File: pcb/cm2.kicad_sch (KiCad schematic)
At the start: 614 parts, among them J1 top left, J2 bottom left, J3 Raspberry_Pi_2_3, J4 Screw_Terminal_01x02, J5 Screw_Terminal_01x02, U1 HT1632C-52LQFP, U2 HT1632C-52LQFP

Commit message: update to v6.0
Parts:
- C1, C11, C12, C2: symbol Device:CP1 -> Device:C_Polarized_Small_US
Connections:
- net +5V: now also C1.1, C11.1, C12.1, C2.1
- net GND: now also C1.2, C11.2, C12.2, C2.2
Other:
- note added: "Design for either SMT or TH large caps, no need to install both! (DNP either C1, C2 or CX, CY)"
- note added: "Designed for two boards to be plugged together so that ~{CS2} and ~{CS3} of the left board (with the RPi) become ~{CS0} and ~{CS1} of the right board."
- note added: "For historical accuracy, ensure LEDS have a spectral center > 635 nM Drivers only supply ~10 mA so high-brightness LEDS such as LUMEX SSL-LX5093SID are recommended for applications with high ambient light."
- note added: "Only J1 or J2 need be installed on one board."
- note added: "Power entry: 5VDC Ensure minimum 2A"
- note added: "cm2: LED display inspired by Connection Machine 2021 Jonathan Foote rotormind.com"
- note removed: "Design for either SMT or TH large caps, no need to install both! (DNP either C1, C2 or CX CY)"
- moved on the sheet: J1, J2

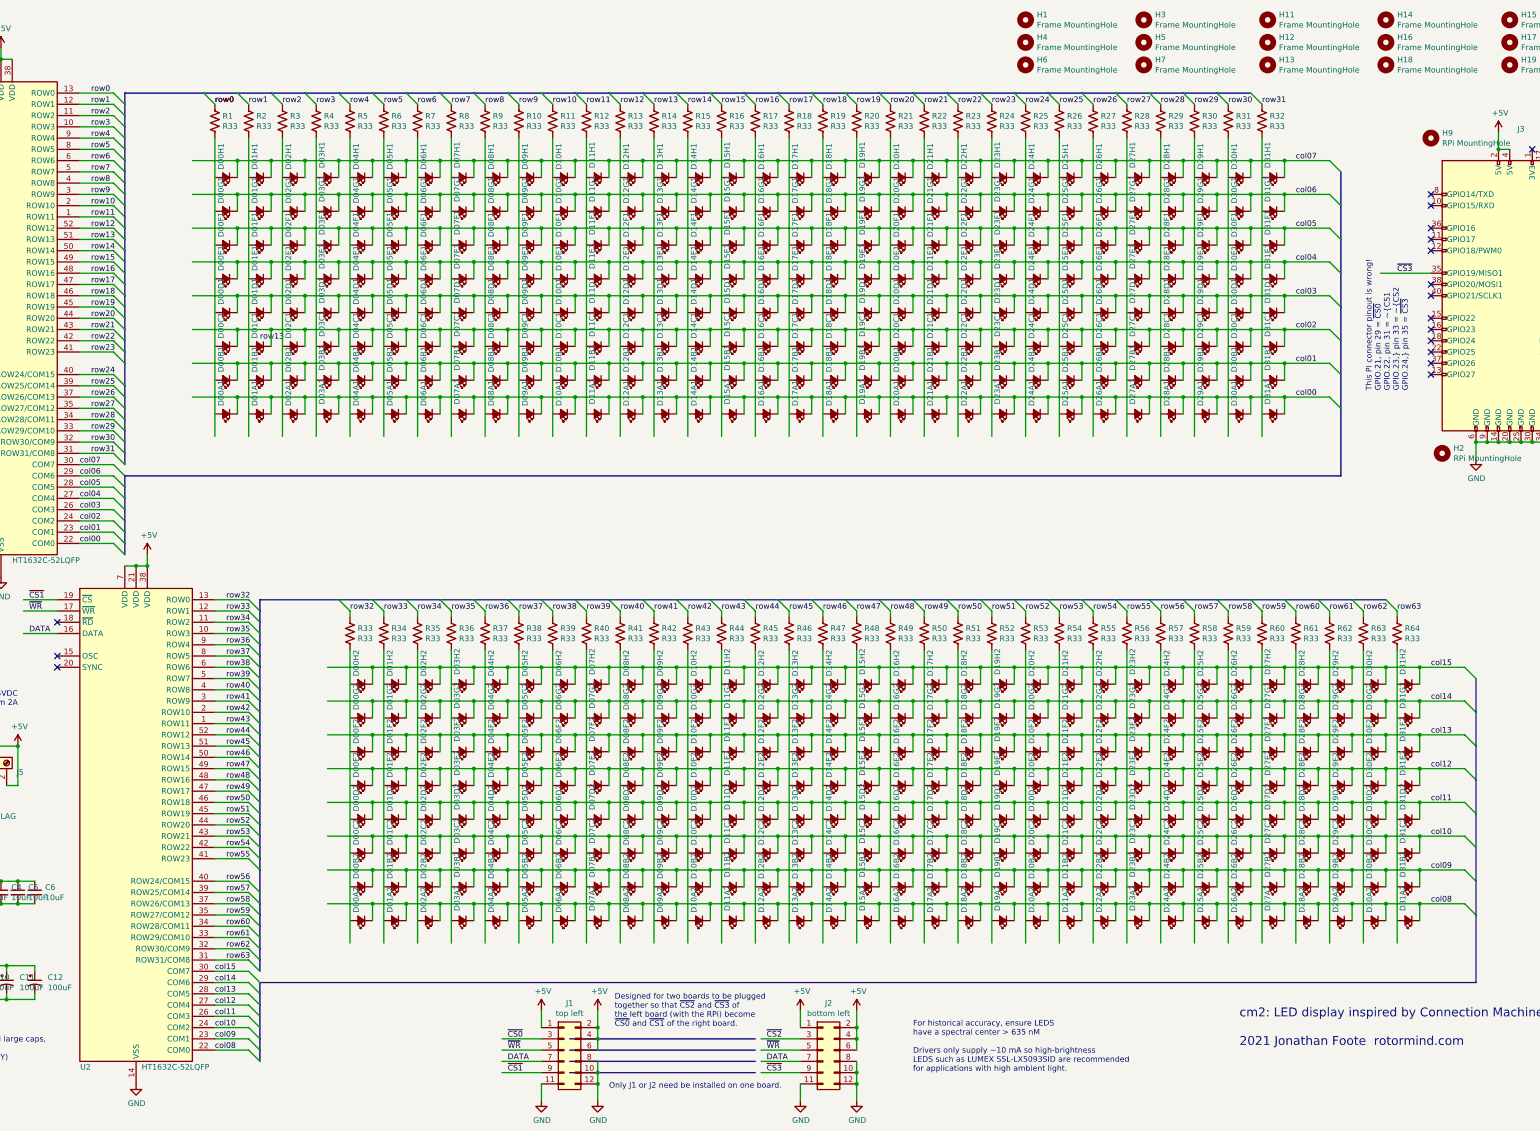
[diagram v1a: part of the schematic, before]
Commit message: fix errors from v6 conversion
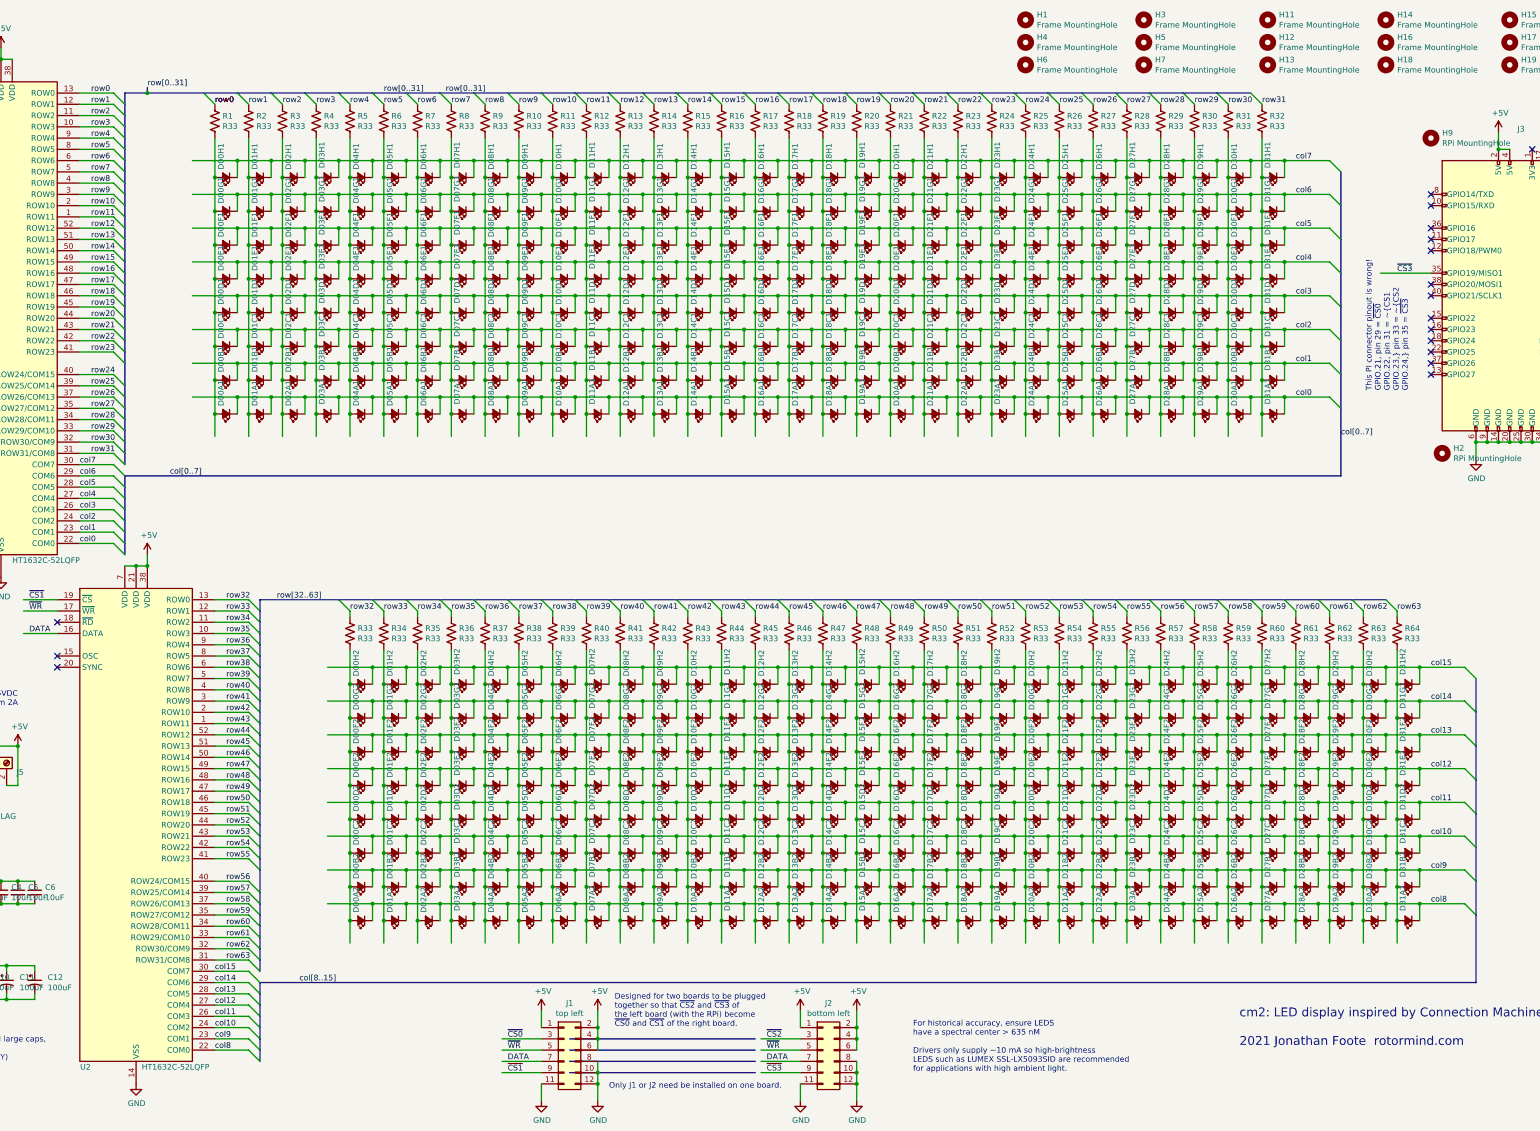
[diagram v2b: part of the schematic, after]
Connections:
- net at D00H1.2 (A): now also D00A1.2 (A), D00B1.2 (A), D00C1.2 (A), D00D1.2 (A), D00E1.2 (A), D00F1.2 (A), D00G1.2 (A), R1.2
- net at D01H1.2 (A): now also D01A1.2 (A), D01B1.2 (A), D01C1.2 (A), D01D1.2 (A), D01E1.2 (A), D01F1.2 (A), D01G1.2 (A), R2.2
- net at D02H1.2 (A): now also D02A1.2 (A), D02B1.2 (A), D02C1.2 (A), D02D1.2 (A), D02E1.2 (A), D02F1.2 (A), D02G1.2 (A), R3.2
- net at D03H1.2 (A): now also D03A1.2 (A), D03B1.2 (A), D03C1.2 (A), D03D1.2 (A), D03E1.2 (A), D03F1.2 (A), D03G1.2 (A), R4.2
- net at D16H1.2 (A): now also D16A1.2 (A), D16B1.2 (A), D16C1.2 (A), D16D1.2 (A), D16E1.2 (A), D16F1.2 (A), D16G1.2 (A), R17.2
- net at D19H1.2 (A): now also D19A1.2 (A), D19B1.2 (A), D19C1.2 (A), D19D1.2 (A), D19E1.2 (A), D19F1.2 (A), D19G1.2 (A), R20.2
- net at D18H1.2 (A): now also D18A1.2 (A), D18B1.2 (A), D18C1.2 (A), D18D1.2 (A), D18E1.2 (A), D18F1.2 (A), D18G1.2 (A), R19.2
- net at D17H1.2 (A): now also D17A1.2 (A), D17B1.2 (A), D17C1.2 (A), D17D1.2 (A), D17E1.2 (A), D17F1.2 (A), D17G1.2 (A), R18.2
- net at D20H1.2 (A): now also D20A1.2 (A), D20B1.2 (A), D20C1.2 (A), D20D1.2 (A), D20E1.2 (A), D20F1.2 (A), D20G1.2 (A), R21.2
- net at D23H1.2 (A): now also D23A1.2 (A), D23B1.2 (A), D23C1.2 (A), D23D1.2 (A), D23E1.2 (A), D23F1.2 (A), D23G1.2 (A), R24.2
- net at D22H1.2 (A): now also D22A1.2 (A), D22B1.2 (A), D22C1.2 (A), D22D1.2 (A), D22E1.2 (A), D22F1.2 (A), D22G1.2 (A), R23.2
- net at D21H1.2 (A): now also D21A1.2 (A), D21B1.2 (A), D21C1.2 (A), D21D1.2 (A), D21E1.2 (A), D21F1.2 (A), D21G1.2 (A), R22.2
- net at D24H1.2 (A): now also D24A1.2 (A), D24B1.2 (A), D24C1.2 (A), D24D1.2 (A), D24E1.2 (A), D24F1.2 (A), D24G1.2 (A), R25.2
- net at D27H1.2 (A): now also D27A1.2 (A), D27B1.2 (A), D27C1.2 (A), D27D1.2 (A), D27E1.2 (A), D27F1.2 (A), D27G1.2 (A), R28.2
- net at D26H1.2 (A): now also D26A1.2 (A), D26B1.2 (A), D26C1.2 (A), D26D1.2 (A), D26E1.2 (A), D26F1.2 (A), D26G1.2 (A), R27.2
- net at D25H1.2 (A): now also D25A1.2 (A), D25B1.2 (A), D25C1.2 (A), D25D1.2 (A), D25E1.2 (A), D25F1.2 (A), D25G1.2 (A), R26.2
- net at D28H1.2 (A): now also D28A1.2 (A), D28B1.2 (A), D28C1.2 (A), D28D1.2 (A), D28E1.2 (A), D28F1.2 (A), D28G1.2 (A), R29.2
- net at D31H1.2 (A): now also D31A1.2 (A), D31B1.2 (A), D31C1.2 (A), D31D1.2 (A), D31E1.2 (A), D31F1.2 (A), D31G1.2 (A), R32.2
- net at D30H1.2 (A): now also D30A1.2 (A), D30B1.2 (A), D30C1.2 (A), D30D1.2 (A), D30E1.2 (A), D30F1.2 (A), D30G1.2 (A), R31.2
- net at D29H1.2 (A): now also D29A1.2 (A), D29B1.2 (A), D29C1.2 (A), D29D1.2 (A), D29E1.2 (A), D29F1.2 (A), D29G1.2 (A), R30.2
- net at D04H1.2 (A): now also D04A1.2 (A), D04B1.2 (A), D04C1.2 (A), D04D1.2 (A), D04E1.2 (A), D04F1.2 (A), D04G1.2 (A), R5.2
- net at D07H1.2 (A): now also D07A1.2 (A), D07B1.2 (A), D07C1.2 (A), D07D1.2 (A), D07E1.2 (A), D07F1.2 (A), D07G1.2 (A), R8.2
- net at D06H1.2 (A): now also D06A1.2 (A), D06B1.2 (A), D06C1.2 (A), D06D1.2 (A), D06E1.2 (A), D06F1.2 (A), D06G1.2 (A), R7.2
- net at D05H1.2 (A): now also D05A1.2 (A), D05B1.2 (A), D05C1.2 (A), D05D1.2 (A), D05E1.2 (A), D05F1.2 (A), D05G1.2 (A), R6.2
- net at D08H1.2 (A): now also D08A1.2 (A), D08B1.2 (A), D08C1.2 (A), D08D1.2 (A), D08E1.2 (A), D08F1.2 (A), D08G1.2 (A), R9.2
- net at D11H1.2 (A): now also D11A1.2 (A), D11B1.2 (A), D11C1.2 (A), D11D1.2 (A), D11E1.2 (A), D11F1.2 (A), D11G1.2 (A), R12.2
- net at D10H1.2 (A): now also D10A1.2 (A), D10B1.2 (A), D10C1.2 (A), D10D1.2 (A), D10E1.2 (A), D10F1.2 (A), D10G1.2 (A), R11.2
- net at D09H1.2 (A): now also D09A1.2 (A), D09B1.2 (A), D09C1.2 (A), D09D1.2 (A), D09E1.2 (A), D09F1.2 (A), D09G1.2 (A), R10.2
- net at D12H1.2 (A): now also D12A1.2 (A), D12B1.2 (A), D12C1.2 (A), D12D1.2 (A), D12E1.2 (A), D12F1.2 (A), D12G1.2 (A), R13.2
- net at D15H1.2 (A): now also D15A1.2 (A), D15B1.2 (A), D15C1.2 (A), D15D1.2 (A), D15E1.2 (A), D15F1.2 (A), D15G1.2 (A), R16.2
- net at D14H1.2 (A): now also D14A1.2 (A), D14B1.2 (A), D14C1.2 (A), D14D1.2 (A), D14E1.2 (A), D14F1.2 (A), D14G1.2 (A), R15.2
- net at D13H1.2 (A): now also D13A1.2 (A), D13B1.2 (A), D13C1.2 (A), D13D1.2 (A), D13E1.2 (A), D13F1.2 (A), D13G1.2 (A), R14.2
- net at D00H2.2 (A): now also D00A2.2 (A), D00B2.2 (A), D00C2.2 (A), D00D2.2 (A), D00E2.2 (A), D00F2.2 (A), D00G2.2 (A), R33.2
- net at D03H2.2 (A): now also D03A2.2 (A), D03B2.2 (A), D03C2.2 (A), D03D2.2 (A), D03E2.2 (A), D03F2.2 (A), D03G2.2 (A), R36.2
- net at D02H2.2 (A): now also D02A2.2 (A), D02B2.2 (A), D02C2.2 (A), D02D2.2 (A), D02E2.2 (A), D02F2.2 (A), D02G2.2 (A), R35.2
- net at D01H2.2 (A): now also D01A2.2 (A), D01B2.2 (A), D01C2.2 (A), D01D2.2 (A), D01E2.2 (A), D01F2.2 (A), D01G2.2 (A), R34.2
- net at D04H2.2 (A): now also D04A2.2 (A), D04B2.2 (A), D04C2.2 (A), D04D2.2 (A), D04E2.2 (A), D04F2.2 (A), D04G2.2 (A), R37.2
- net at D07H2.2 (A): now also D07A2.2 (A), D07B2.2 (A), D07C2.2 (A), D07D2.2 (A), D07E2.2 (A), D07F2.2 (A), D07G2.2 (A), R40.2
- net at D06H2.2 (A): now also D06A2.2 (A), D06B2.2 (A), D06C2.2 (A), D06D2.2 (A), D06E2.2 (A), D06F2.2 (A), D06G2.2 (A), R39.2
- net at D05H2.2 (A): now also D05A2.2 (A), D05B2.2 (A), D05C2.2 (A), D05D2.2 (A), D05E2.2 (A), D05F2.2 (A), D05G2.2 (A), R38.2
- net at D08H2.2 (A): now also D08A2.2 (A), D08B2.2 (A), D08C2.2 (A), D08D2.2 (A), D08E2.2 (A), D08F2.2 (A), D08G2.2 (A), R41.2
- net at D11H2.2 (A): now also D11A2.2 (A), D11B2.2 (A), D11C2.2 (A), D11D2.2 (A), D11E2.2 (A), D11F2.2 (A), D11G2.2 (A), R44.2
- net at D10H2.2 (A): now also D10A2.2 (A), D10B2.2 (A), D10C2.2 (A), D10D2.2 (A), D10E2.2 (A), D10F2.2 (A), D10G2.2 (A), R43.2
- net at D09H2.2 (A): now also D09A2.2 (A), D09B2.2 (A), D09C2.2 (A), D09D2.2 (A), D09E2.2 (A), D09F2.2 (A), D09G2.2 (A), R42.2
- net at D12H2.2 (A): now also D12A2.2 (A), D12B2.2 (A), D12C2.2 (A), D12D2.2 (A), D12E2.2 (A), D12F2.2 (A), D12G2.2 (A), R45.2
- net at D15H2.2 (A): now also D15A2.2 (A), D15B2.2 (A), D15C2.2 (A), D15D2.2 (A), D15E2.2 (A), D15F2.2 (A), D15G2.2 (A), R48.2
- net at D14H2.2 (A): now also D14A2.2 (A), D14B2.2 (A), D14C2.2 (A), D14D2.2 (A), D14E2.2 (A), D14F2.2 (A), D14G2.2 (A), R47.2
- net at D13H2.2 (A): now also D13A2.2 (A), D13B2.2 (A), D13C2.2 (A), D13D2.2 (A), D13E2.2 (A), D13F2.2 (A), D13G2.2 (A), R46.2
- net at D29G2.2 (A): now also D29A2.2 (A), D29B2.2 (A), D29C2.2 (A), D29D2.2 (A), D29E2.2 (A), D29F2.2 (A), D29H2.2 (A), R62.2
- net at D30G2.2 (A): now also D30A2.2 (A), D30B2.2 (A), D30C2.2 (A), D30D2.2 (A), D30E2.2 (A), D30F2.2 (A), D30H2.2 (A), R63.2
- net at D31G2.2 (A): now also D31A2.2 (A), D31B2.2 (A), D31C2.2 (A), D31D2.2 (A), D31E2.2 (A), D31F2.2 (A), D31H2.2 (A), R64.2
- net at D28G2.2 (A): now also D28A2.2 (A), D28B2.2 (A), D28C2.2 (A), D28D2.2 (A), D28E2.2 (A), D28F2.2 (A), D28H2.2 (A), R61.2
- net at D25G2.2 (A): now also D25A2.2 (A), D25B2.2 (A), D25C2.2 (A), D25D2.2 (A), D25E2.2 (A), D25F2.2 (A), D25H2.2 (A), R58.2
- net at D26G2.2 (A): now also D26A2.2 (A), D26B2.2 (A), D26C2.2 (A), D26D2.2 (A), D26E2.2 (A), D26F2.2 (A), D26H2.2 (A), R59.2
- net at D27G2.2 (A): now also D27A2.2 (A), D27B2.2 (A), D27C2.2 (A), D27D2.2 (A), D27E2.2 (A), D27F2.2 (A), D27H2.2 (A), R60.2
- net at D24G2.2 (A): now also D24A2.2 (A), D24B2.2 (A), D24C2.2 (A), D24D2.2 (A), D24E2.2 (A), D24F2.2 (A), D24H2.2 (A), R57.2
- net at D21G2.2 (A): now also D21A2.2 (A), D21B2.2 (A), D21C2.2 (A), D21D2.2 (A), D21E2.2 (A), D21F2.2 (A), D21H2.2 (A), R54.2
- net at D22G2.2 (A): now also D22A2.2 (A), D22B2.2 (A), D22C2.2 (A), D22D2.2 (A), D22E2.2 (A), D22F2.2 (A), D22H2.2 (A), R55.2
- net at D23G2.2 (A): now also D23A2.2 (A), D23B2.2 (A), D23C2.2 (A), D23D2.2 (A), D23E2.2 (A), D23F2.2 (A), D23H2.2 (A), R56.2
- net at D20G2.2 (A): now also D20A2.2 (A), D20B2.2 (A), D20C2.2 (A), D20D2.2 (A), D20E2.2 (A), D20F2.2 (A), D20H2.2 (A), R53.2
- net at D17G2.2 (A): now also D17A2.2 (A), D17B2.2 (A), D17C2.2 (A), D17D2.2 (A), D17E2.2 (A), D17F2.2 (A), D17H2.2 (A), R50.2
- net at D18G2.2 (A): now also D18A2.2 (A), D18B2.2 (A), D18C2.2 (A), D18D2.2 (A), D18E2.2 (A), D18F2.2 (A), D18H2.2 (A), R51.2
- net at D19G2.2 (A): now also D19A2.2 (A), D19B2.2 (A), D19C2.2 (A), D19D2.2 (A), D19E2.2 (A), D19F2.2 (A), D19H2.2 (A), R52.2
- net at D16G2.2 (A): now also D16A2.2 (A), D16B2.2 (A), D16C2.2 (A), D16D2.2 (A), D16E2.2 (A), D16F2.2 (A), D16H2.2 (A), R49.2
- net col00 renamed col0
- net col01 renamed col1
- net col02 renamed col2
- net col03 renamed col3
- net col04 renamed col4
- net col05 renamed col5
- net col06 renamed col6
- net col07 renamed col7
- net col08 renamed col8
- net col09 renamed col9
